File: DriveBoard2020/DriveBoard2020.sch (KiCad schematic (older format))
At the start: 66 parts, among them SW0 SW_SPST, SW1 SW_Push, SW3 SW_Push, SW5 SW_Push, SW7 SW_Push, SW8 SW_Push, SW9 SW_Push, U1 MAX_3232, U2 MAX_3232, U3 OKI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

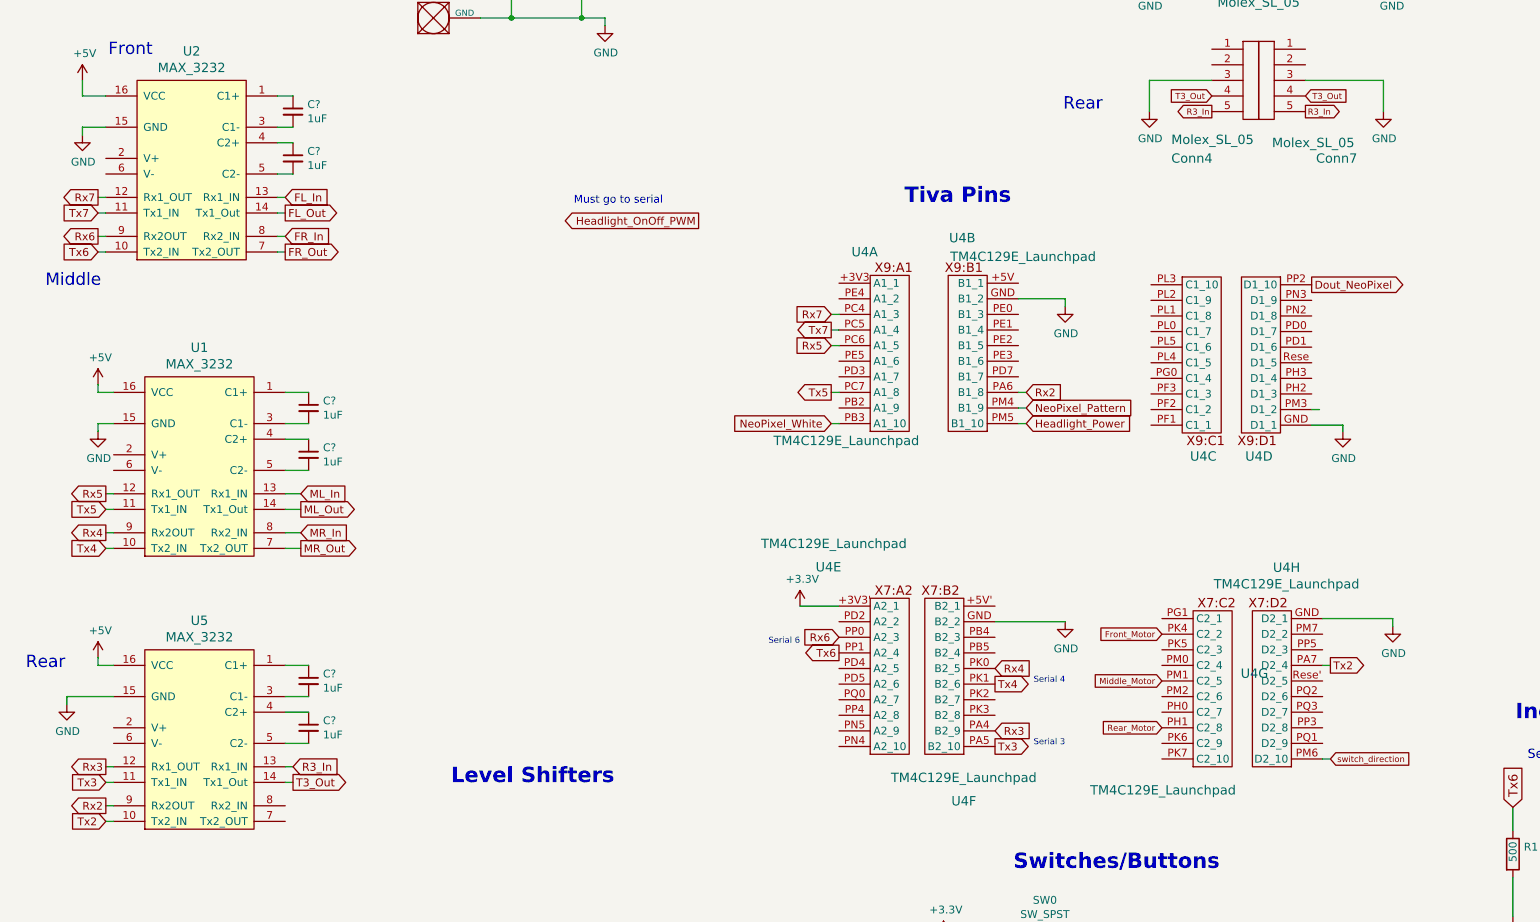
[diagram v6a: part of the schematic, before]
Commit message: corrected capacitor values
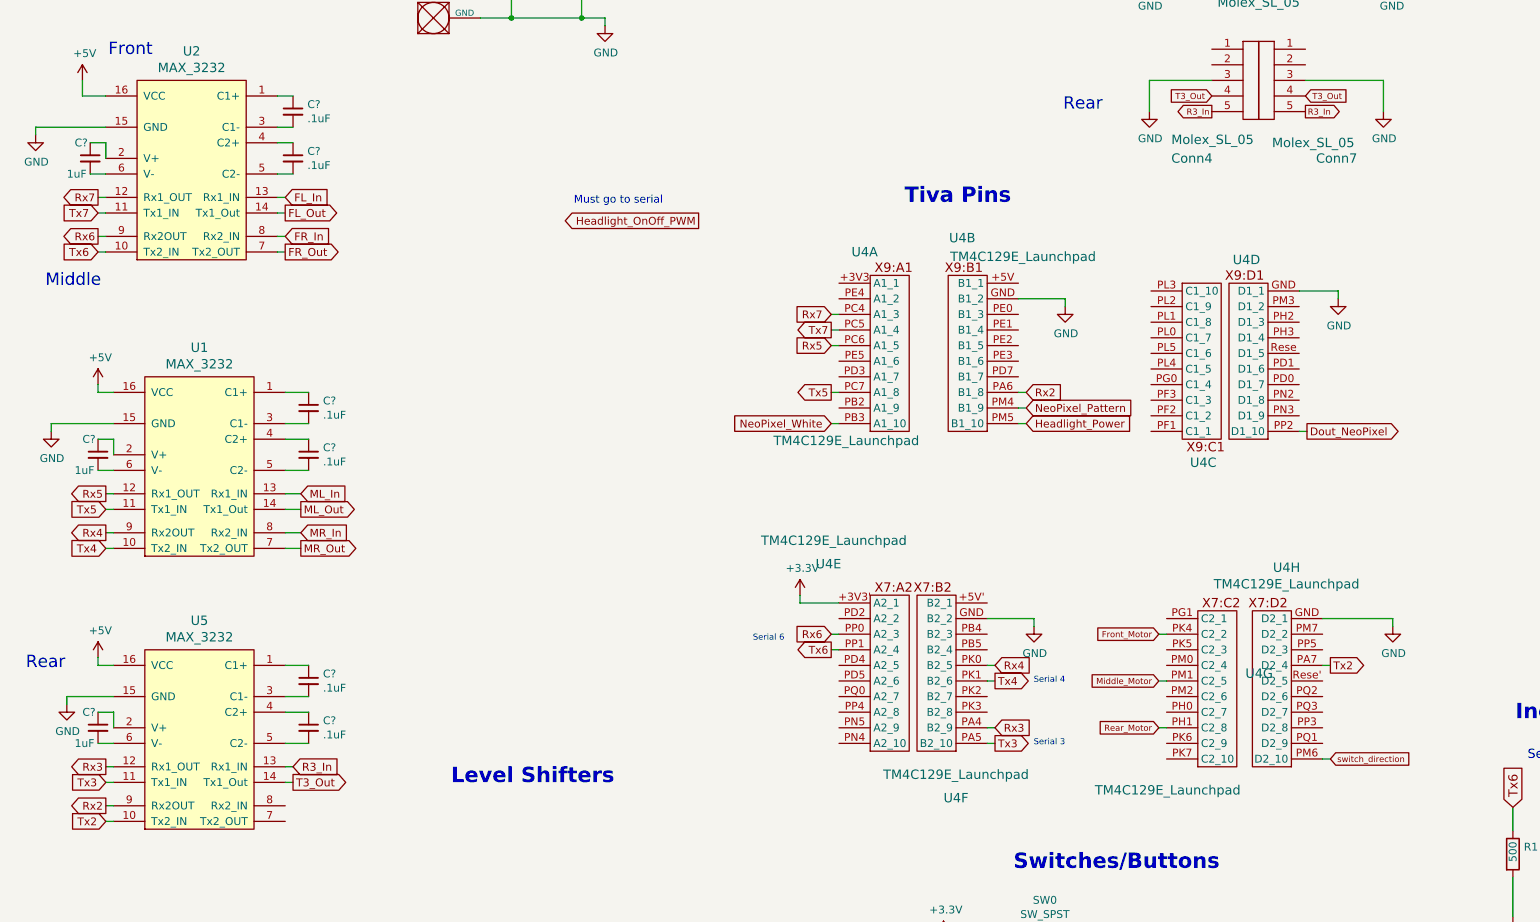
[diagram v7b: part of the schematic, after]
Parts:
- added C? (x3): 1uF, symbol Device:C_Small
- C? (x6): value 1uF -> .1uF
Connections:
- net at U2.2 (V+): now also C?.1
- net at U2.6 (V-): now also C?.2
- net at U5.2 (V+): now also C?.1
- net at U5.6 (V-): now also C?.2
- net at U1.2 (V+): now also C?.1
- net at U1.6 (V-): now also C?.2
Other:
- moved on the sheet: U4C, U4D, U4E, U4F, U4G

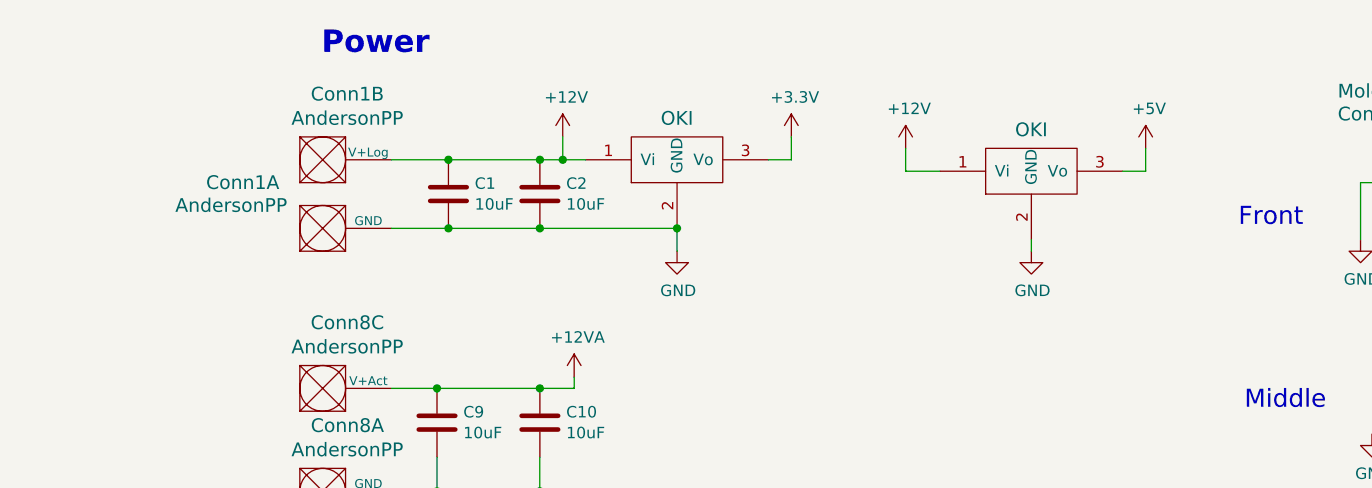
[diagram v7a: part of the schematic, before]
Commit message: added capacitors to OKI's
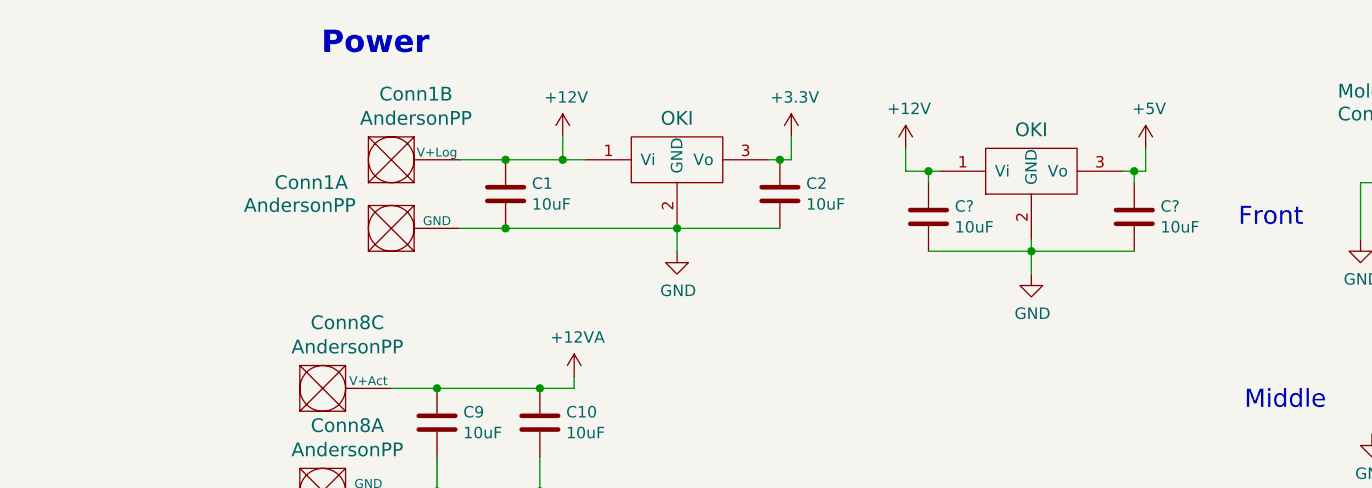
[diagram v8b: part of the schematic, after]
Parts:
- added C? (x2): 10uF, Capacitor_SMD:C_0603_1608Metric_Pad1.05x0.95mm_HandSolder, symbol Device:C
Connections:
- net +12V: now also C?.1; no longer C2.1
- net +3V3: now also C2.1
- net +5V: now also C?.1
- net GND: now also C?.2, C?.2
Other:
- moved on the sheet: C1, C2, Conn1A, Conn1B
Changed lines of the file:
@@
 L DriveBoard2020-rescue:AndersonPP-MRDT_Connectors-DriveBoard2020-rescue Conn1
 U 2 1 5D9F5218
-P 5400 1300
-F 0 "Conn1" H 5608 1687 60  0000 C CNN
-F 1 "AndersonPP" H 5608 1581 60  0000 C CNN
-F 2 "MRDT_Connectors:Anderson_2_Horizontal_Side_by_Side" H 5250 750 60  0001 C CNN
-F 3 "" H 5250 750 60  0001 C CNN
-	2    5400 1300
+P 5700 1300
+F 0 "Conn1" H 5908 1687 60  0000 C CNN
+F 1 "AndersonPP" H 5908 1581 60  0000 C CNN
+F 2 "MRDT_Connectors:Anderson_2_Horizontal_Side_by_Side" H 5550 750 60  0001 C CNN
+F 3 "" H 5550 750 60  0001 C CNN
+	2    5700 1300
 	1    0    0    -1
 $EndComp
@@
 L Device:C C2
 U 1 1 5D994283
-P 6450 1350
-F 0 "C2" H 6565 1396 50  0000 L CNN
-F 1 "10uF" H 6565 1305 50  0000 L CNN
-F 2 "Capacitor_SMD:C_0603_1608Metric_Pad1.05x0.95mm_HandSolder" H 6488 1200 50  0001 C CNN
-F 3 "~" H 6450 1350 50  0001 C CNN
-	1    6450 1350
+P 7500 1350
+F 0 "C2" H 7615 1396 50  0000 L CNN
+F 1 "10uF" H 7615 1305 50  0000 L CNN
+F 2 "Capacitor_SMD:C_0603_1608Metric_Pad1.05x0.95mm_HandSolder" H 7538 1200 50  0001 C CNN
+F 3 "~" H 7500 1350 50  0001 C CNN
+	1    7500 1350
 	1    0    0    -1
 $EndComp
@@
 L Device:C C1
 U 1 1 5D990CA8
-P 6050 1350
-F 0 "C1" H 6165 1396 50  0000 L CNN
-F 1 "10uF" H 6165 1305 50  0000 L CNN
-F 2 "Capacitor_SMD:C_0603_1608Metric_Pad1.05x0.95mm_HandSolder" H 6088 1200 50  0001 C CNN
-F 3 "~" H 6050 1350 50  0001 C CNN
-	1    6050 1350
+P 6300 1350
+F 0 "C1" H 6415 1396 50  0000 L CNN
+F 1 "10uF" H 6415 1305 50  0000 L CNN
+F 2 "Capacitor_SMD:C_0603_1608Metric_Pad1.05x0.95mm_HandSolder" H 6338 1200 50  0001 C CNN
+F 3 "~" H 6300 1350 50  0001 C CNN
+	1    6300 1350
 	1    0    0    -1
 $EndComp
@@
 L DriveBoard2020-rescue:AndersonPP-MRDT_Connectors-DriveBoard2020-rescue Conn1
 U 1 1 5D9156E9
-P 5400 1600
-F 0 "Conn1" H 5150 1900 60  0000 C CNN
-F 1 "AndersonPP" H 5100 1800 60  0000 C CNN
-F 2 "MRDT_Connectors:Anderson_2_Horizontal_Side_by_Side" H 5250 1050 60  0001 C CNN
-F 3 "" H 5250 1050 60  0001 C CNN
-	1    5400 1600
+P 5700 1600
+F 0 "Conn1" H 5450 1900 60  0000 C CNN
+F 1 "AndersonPP" H 5400 1800 60  0000 C CNN
+F 2 "MRDT_Connectors:Anderson_2_Horizontal_Side_by_Side" H 5550 1050 60  0001 C CNN
+F 3 "" H 5550 1050 60  0001 C CNN
+	1    5700 1600
 	1    0    0    -1
 $EndComp
@@
 L power:GND #PWR0139
 U 1 1 5E77D4FB
-P 8600 1600
-F 0 "#PWR0139" H 8600 1350 50  0001 C CNN
-F 1 "GND" H 8605 1427 50  0000 C CNN
-F 2 "" H 8600 1600 50  0001 C CNN
-F 3 "" H 8600 1600 50  0001 C CNN
-	1    8600 1600
+P 8600 1700
+F 0 "#PWR0139" H 8600 1450 50  0001 C CNN
+F 1 "GND" H 8605 1527 50  0000 C CNN
+F 2 "" H 8600 1700 50  0001 C CNN
+F 3 "" H 8600 1700 50  0001 C CNN
+	1    8600 1700
 	1    0    0    -1
 $EndComp
@@
 	9100 1150 9100 1250
 Wire Wire Line
-	9100 1250 9000 1250
+	9100 1250 9050 1250
 Wire Wire Line
 	8050 1150 8050 1250
 Wire Wire Line
-	8050 1250 8200 1250
+	8050 1250 8150 1250
 Wire Wire Line
 	8600 1550 8600 1600
@@
 Connection ~ 6000 2200
 Wire Wire Line
-	5800 1200 6050 1200
-Connection ~ 6050 1200
-Wire Wire Line
-	6050 1200 6450 1200
-Wire Wire Line
-	5800 1500 6050 1500
-Connection ~ 6050 1500
-Wire Wire Line
-	6050 1500 6450 1500
-Wire Wire Line
-	6450 1500 7050 1500
-Connection ~ 6450 1500
-Wire Wire Line
 	7050 1500 7050 1600
 Connection ~ 7050 1500
 Wire Wire Line
 	6650 1200 6550 1200
-Connection ~ 6450 1200
 Wire Wire Line
 	6550 1100 6550 1200
 Connection ~ 6550 1200
 Wire Wire Line
-	6550 1200 6450 1200
-Wire Wire Line
-	7450 1200 7550 1200
+	7450 1200 7500 1200
 Wire Wire Line
 	7550 1200 7550 1100
@@
 	1    0    0    -1
 $EndComp
+Connection ~ 7500 1200
+Wire Wire Line
+	7500 1200 7550 1200
+Wire Wire Line
+	7050 1500 7500 1500
+Wire Wire Line
+	6300 1200 6550 1200
+Wire Wire Line
+	6300 1500 7050 1500
+Wire Wire Line
+	6100 1200 6300 1200
+Connection ~ 6300 1200
+Wire Wire Line
+	6100 1500 6300 1500
+Connection ~ 6300 1500
+$Comp
+L Device:C C?
+U 1 1 5E218078
+P 8150 1450
+F 0 "C?" H 8265 1496 50  0000 L CNN
+F 1 "10uF" H 8265 1405 50  0000 L CNN
+F 2 "Capacitor_SMD:C_0603_1608Metric_Pad1.05x0.95mm_HandSolder" H 8188 1300 50  0001 C CNN
+F 3 "~" H 8150 1450 50  0001 C CNN
+	1    8150 1450
+	1    0    0    -1
+$EndComp
+$Comp
+L Device:C C?
+U 1 1 5E2189BA
+P 9050 1450
+F 0 "C?" H 9165 1496 50  0000 L CNN
+F 1 "10uF" H 9165 1405 50  0000 L CNN
+F 2 "Capacitor_SMD:C_0603_1608Metric_Pad1.05x0.95mm_HandSolder" H 9088 1300 50  0001 C CNN
+F 3 "~" H 9050 1450 50  0001 C CNN
+	1    9050 1450
+	1    0    0    -1
+$EndComp
+Wire Wire Line
+	8150 1250 8150 1300
+Connection ~ 8150 1250
+Wire Wire Line
+	8150 1250 8200 1250
+Wire Wire Line
+	8150 1600 8600 1600
+Connection ~ 8600 1600
+Wire Wire Line
+	8600 1600 9050 1600
+Wire Wire Line
+	8600 1600 8600 1700
+Wire Wire Line
+	9050 1300 9050 1250
+Connection ~ 9050 1250
+Wire Wire Line
+	9050 1250 9000 1250
 $EndSCHEMATC
